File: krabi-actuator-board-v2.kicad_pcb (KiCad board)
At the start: 2 copper layers, 101.6 x 53.3 mm, 18 parts, among them J1 Power, J2 PWM, J3 Analog, J4 PWM, J5 Analog, J6 Communication, J7 Digital, J8 Conn_01x02_Pin

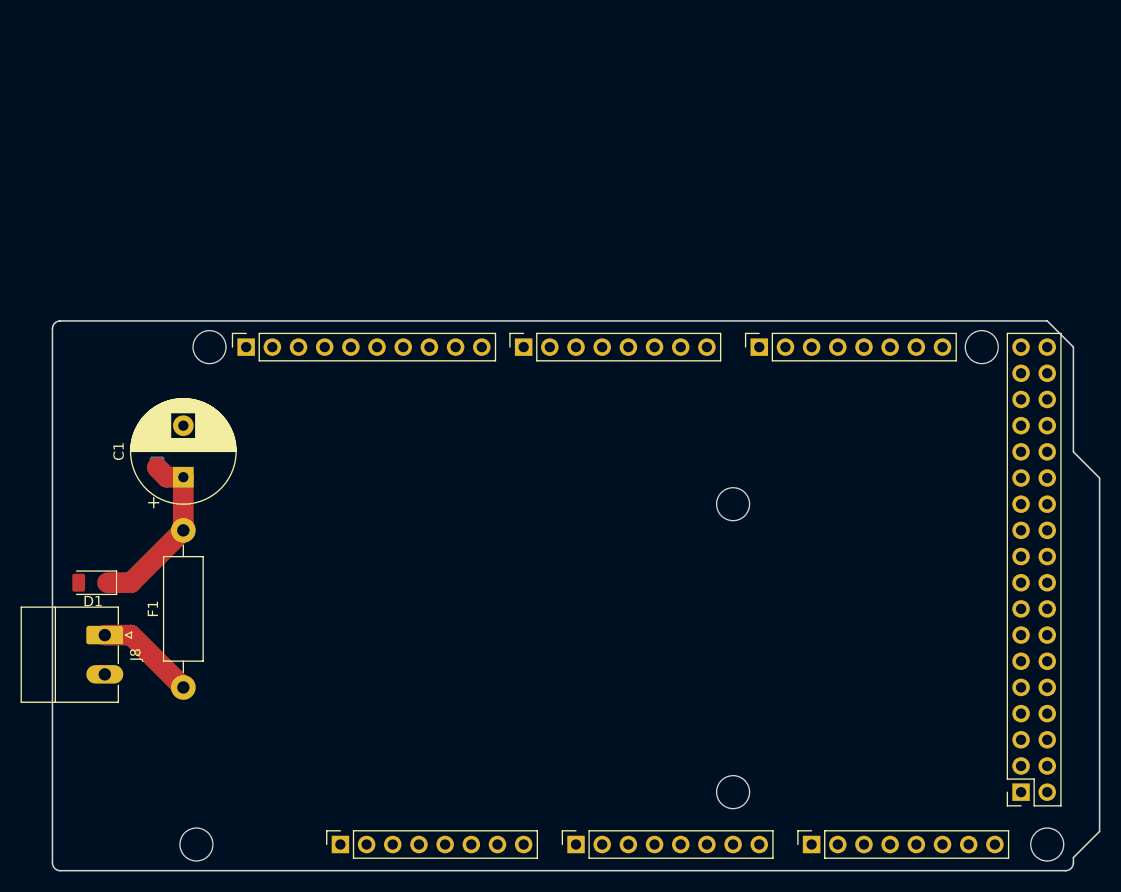
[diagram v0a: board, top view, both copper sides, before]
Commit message: Full command of the servos 6V power
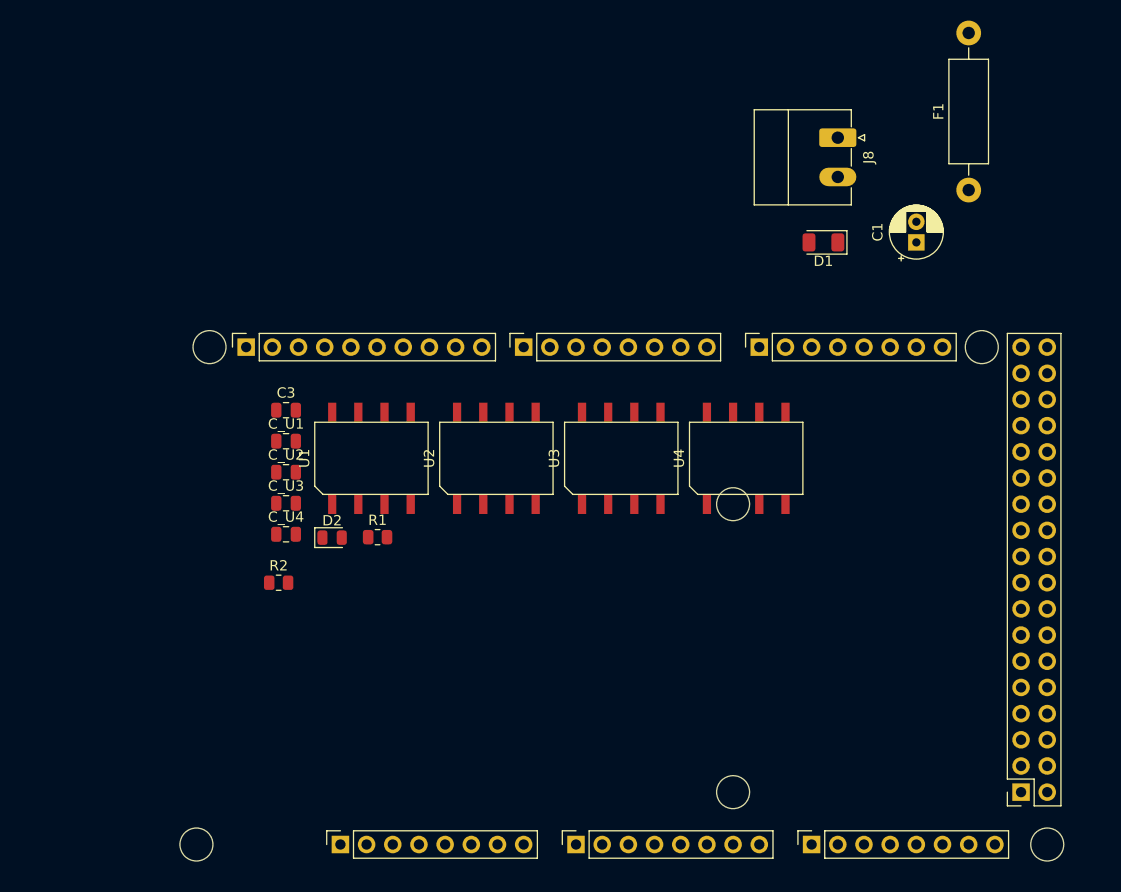
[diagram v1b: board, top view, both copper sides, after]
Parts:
- removed C2: C, Capacitor_SMD:C_0805_2012Metric
- added C3: 100nF, Capacitor_SMD:C_0805_2012Metric, F.Cu at (122.7, 55.3)
- added C_U1: 10pF, Capacitor_SMD:C_0805_2012Metric, F.Cu at (122.7, 58.3)
- added C_U2: 10pF, Capacitor_SMD:C_0805_2012Metric, F.Cu at (122.7, 61.3)
- added C_U3: 10pF, Capacitor_SMD:C_0805_2012Metric, F.Cu at (122.7, 64.3)
- added C_U4: 10pF, Capacitor_SMD:C_0805_2012Metric, F.Cu at (122.7, 67.4)
- added D2: LED, LED_SMD:LED_0805_2012Metric, F.Cu at (127.1, 67.7)
- added R1: 120, Resistor_SMD:R_0805_2012Metric, F.Cu at (131.5, 67.6)
- added R2: 0.01, Resistor_SMD:R_0805_2012Metric, F.Cu at (121.9, 72.1)
- added U1: XGZP6897D_differential_pressure_sensor, Krabi:SOIC-8-11mmx7mm outside pad 1.9, F.Cu at (130.9, 60.0)
- added U2: XGZP6897D_differential_pressure_sensor, Krabi:SOIC-8-11mmx7mm outside pad 1.9, F.Cu at (143.1, 60.0)
- added U3: XGZP6897D_differential_pressure_sensor, Krabi:SOIC-8-11mmx7mm outside pad 1.9, F.Cu at (155.2, 60.0)
- added U4: XGZP6897D_differential_pressure_sensor, Krabi:SOIC-8-11mmx7mm outside pad 1.9, F.Cu at (167.3, 60.0)
- C1: value 10µF -> 10mF; footprint Capacitor_THT:CP_Radial_D10.0mm_P5.00mm -> Capacitor_THT:CP_Radial_D5.0mm_P2.00mm
- moved F1 90.2 mm to (188.9, 34.0)
- moved J8 85.9 mm to (176.2, 28.9)
- moved D1 78.2 mm to (174.8, 39.0)
- moved C1 74.7 mm to (183.8, 39.0)
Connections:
- net /SCL/21 renamed SCL
- net /SDA/20 renamed SDA
- C1 pad 2: GNF_POWER -> GND
- D1 pad 2: GNF_POWER -> GND
- J8 pad 2: GNF_POWER -> GND
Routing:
- net 12_V: track 17.6 -> 0.00 mm
- net Net-(J8-Pin_1): track 9.72 -> 0.00 mm
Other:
- board outline removed

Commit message: Fixing bad association and symbols*
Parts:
- removed C_U3, C_U4: 10pF, Capacitor_SMD:C_0805_2012Metric
- removed U3, U4: XGZP6897D_differential_pressure_sensor, Krabi:SOIC-8-11mmx7mm outside pad 1.9
- added CFF_VR1: 3.3nF, Capacitor_SMD:C_0805_2012Metric, F.Cu at (-96.9, -99.1)
- added CFF_VR2: 3.3nF, Capacitor_SMD:C_0805_2012Metric, F.Cu at (-96.9, -96.1)
- added C_SV1: 100nF, Capacitor_SMD:C_0805_2012Metric, F.Cu at (-96.9, -93.1)
- added C_SV10: 100nF, Capacitor_SMD:C_0805_2012Metric, F.Cu at (-88.0, -96.1)
- added C_SV11: 100nF, Capacitor_SMD:C_0805_2012Metric, F.Cu at (-88.0, -93.1)
- added C_SV12: 100nF, Capacitor_SMD:C_0805_2012Metric, F.Cu at (-88.0, -90.1)
- added C_SV2: 100nF, Capacitor_SMD:C_0805_2012Metric, F.Cu at (-96.9, -90.1)
- added C_SV3: 100nF, Capacitor_SMD:C_0805_2012Metric, F.Cu at (-96.9, -87.1)
- added C_SV4: 100nF, Capacitor_SMD:C_0805_2012Metric, F.Cu at (-92.5, -99.1)
- added C_SV5: 100nF, Capacitor_SMD:C_0805_2012Metric, F.Cu at (-92.5, -96.1)
- added C_SV6: 100nF, Capacitor_SMD:C_0805_2012Metric, F.Cu at (-92.5, -93.1)
- added C_SV7: 100nF, Capacitor_SMD:C_0805_2012Metric, F.Cu at (-92.5, -90.1)
- added C_SV8: 100nF, Capacitor_SMD:C_0805_2012Metric, F.Cu at (-92.5, -87.1)
- added C_SV9: 100nF, Capacitor_SMD:C_0805_2012Metric, F.Cu at (-88.0, -99.1)
- added C_U5: 10pF, Capacitor_SMD:C_0805_2012Metric, F.Cu at (-85.0, -48.7)
- added C_U6: 10pF, Capacitor_SMD:C_0805_2012Metric, F.Cu at (-85.0, -45.7)
- added Cin_VR1: 470µF, Capacitor_THT:CP_Radial_D5.0mm_P2.00mm, F.Cu at (-83.4, -97.4)
- added Cin_VR2: 470µF, Capacitor_THT:CP_Radial_D5.0mm_P2.00mm, F.Cu at (-83.4, -90.8)
- added Cout_VR1: 470µF, Capacitor_THT:CP_Radial_D13.0mm_P5.00mm, F.Cu at (-126.6, -93.4)
- added Cout_VR2: 470µF, Capacitor_THT:CP_Radial_D13.0mm_P5.00mm, F.Cu at (-126.6, -78.8)
- added D1_VR1: 20V 5A, Diode_SMD:D_0805_2012Metric, F.Cu at (-83.8, -72.2)
- added D1_VR2: 20V 5A, Diode_SMD:D_0805_2012Metric, F.Cu at (-83.8, -69.1)
- added D3: LED, LED_SMD:LED_0805_2012Metric, F.Cu at (-83.8, -75.2)
- added D4: LED, LED_SMD:LED_0805_2012Metric, F.Cu at (-85.0, -42.7)
- added DS_PV1: D_Schottky 20V 1A, Diode_SMD:D_SMA, F.Cu at (-97.6, -36.7)
- added DS_PV2: D_Schottky 20V 1A, Diode_SMD:D_SMA, F.Cu at (-97.6, -32.2)
- added DS_PV3: D_Schottky 20V 1A, Diode_SMD:D_SMA, F.Cu at (-97.6, -27.6)
- added DS_PV4: D_Schottky 20V 1A, Diode_SMD:D_SMA, F.Cu at (-97.6, -23.1)
- added D_LS1: LED, LED_SMD:LED_0805_2012Metric, F.Cu at (-112.8, -37.5)
- added D_LS2: LED, LED_SMD:LED_0805_2012Metric, F.Cu at (-112.8, -34.4)
- added D_PV1: LED, LED_SMD:LED_0805_2012Metric, F.Cu at (-112.8, -31.4)
- added D_PV2: LED, LED_SMD:LED_0805_2012Metric, F.Cu at (-112.8, -28.3)
- added D_PV3: LED, LED_SMD:LED_0805_2012Metric, F.Cu at (-112.8, -25.3)
- added D_PV4: LED, LED_SMD:LED_0805_2012Metric, F.Cu at (-112.8, -22.3)
- added D_S1: LED, LED_SMD:LED_0805_2012Metric, F.Cu at (-112.8, -19.2)
- added D_S10: LED, LED_SMD:LED_0805_2012Metric, F.Cu at (-103.9, -34.4)
- added D_S11: LED, LED_SMD:LED_0805_2012Metric, F.Cu at (-103.9, -31.4)
- added D_S12: LED, LED_SMD:LED_0805_2012Metric, F.Cu at (-103.9, -28.3)
- added D_S2: LED, LED_SMD:LED_0805_2012Metric, F.Cu at (-108.4, -37.5)
- added D_S3: LED, LED_SMD:LED_0805_2012Metric, F.Cu at (-108.4, -34.4)
- added D_S4: LED, LED_SMD:LED_0805_2012Metric, F.Cu at (-108.4, -31.4)
- added D_S5: LED, LED_SMD:LED_0805_2012Metric, F.Cu at (-108.4, -28.3)
- added D_S6: LED, LED_SMD:LED_0805_2012Metric, F.Cu at (-108.4, -25.3)
- added D_S7: LED, LED_SMD:LED_0805_2012Metric, F.Cu at (-108.4, -22.3)
- added D_S8: LED, LED_SMD:LED_0805_2012Metric, F.Cu at (-108.4, -19.2)
- added D_S9: LED, LED_SMD:LED_0805_2012Metric, F.Cu at (-103.9, -37.5)
- added J_PV_1: ~, Connector_JST:JST_PH_B2B-PH-K_1x02_P2.00mm_Vertical, F.Cu at (-128.8, -59.9)
- added J_PV_2: ~, Connector_JST:JST_PH_B2B-PH-K_1x02_P2.00mm_Vertical, F.Cu at (-128.8, -53.3)
- added J_PV_3: ~, Connector_JST:JST_PH_B2B-PH-K_1x02_P2.00mm_Vertical, F.Cu at (-128.8, -46.8)
- added J_PV_4: ~, Connector_JST:JST_PH_B2B-PH-K_1x02_P2.00mm_Vertical, F.Cu at (-128.8, -40.2)
- added L1_VR1: 33µH, Krabi:BOURSPM5022, F.Cu at (-166.6, -57.2)
- added L1_VR2: 33µH, Krabi:BOURSPM5022, F.Cu at (-166.6, -42.1)
- added LED_VR1: LED, LED_SMD:LED_0805_2012Metric, F.Cu at (-83.8, -66.1)
- added LS1: Conn_01x02_Pin, Connector_JST:JST_PH_B2B-PH-K_1x02_P2.00mm_Vertical, F.Cu at (-128.8, -33.7)
- added LS2: Conn_01x02_Pin, Connector_JST:JST_PH_B2B-PH-K_1x02_P2.00mm_Vertical, F.Cu at (-128.8, -27.1)
- added MCP6N11_VR1: G10, Krabi:SOIC-8-1.27x5.4m, F.Cu at (-95.9, -72.5)
- added MCP6N11_VR2: G10, Krabi:SOIC-8-1.27x5.4m, F.Cu at (-89.4, -72.5)
- added Q_LS1: DMN2011UTS, Package_SO:TSSOP-8_4.4x3mm_P0.65mm, F.Cu at (-119.4, -60.3)
- added Q_LS2: DMN2011UTS, Package_SO:TSSOP-8_4.4x3mm_P0.65mm, F.Cu at (-119.4, -55.8)
- added Q_PV1: DMN2011UTS, Package_SO:TSSOP-8_4.4x3mm_P0.65mm, F.Cu at (-119.4, -51.2)
- added Q_PV2: DMN2011UTS, Package_SO:TSSOP-8_4.4x3mm_P0.65mm, F.Cu at (-119.4, -46.7)
- added Q_PV3: DMN2011UTS, Package_SO:TSSOP-8_4.4x3mm_P0.65mm, F.Cu at (-119.4, -42.1)
- added Q_PV4: DMN2011UTS, Package_SO:TSSOP-8_4.4x3mm_P0.65mm, F.Cu at (-119.4, -37.6)
- added R1_VR1: 38.8k, Resistor_SMD:R_0805_2012Metric, F.Cu at (-96.9, -84.1)
- added R1_VR2: 38.8k, Resistor_SMD:R_0805_2012Metric, F.Cu at (-96.9, -81.2)
- added R1_VR3: 50k, Resistor_SMD:R_0805_2012Metric, F.Cu at (-96.9, -78.2)
- added R1_VR4: 100, Resistor_SMD:R_0805_2012Metric, F.Cu at (-92.5, -84.1)
- added R2_VR1: 10k, Resistor_SMD:R_0805_2012Metric, F.Cu at (-92.5, -81.2)
- added R2_VR2: 10k, Resistor_SMD:R_0805_2012Metric, F.Cu at (-92.5, -78.2)
- added R3: 720, Resistor_SMD:R_0805_2012Metric, F.Cu at (-89.4, -48.8)
- added RB_LS1: 1.2k, Resistor_SMD:R_0805_2012Metric, F.Cu at (-112.9, -61.1)
- added RB_LS2: 1.2k, Resistor_SMD:R_0805_2012Metric, F.Cu at (-112.9, -58.2)
- added RB_ON_OFF_ALIM1: 6.65k, Resistor_SMD:R_0805_2012Metric, F.Cu at (-89.4, -45.8)
- added RF_VR1: 50k, Resistor_SMD:R_0805_2012Metric, F.Cu at (-88.1, -84.1)
- added RG_PV1: 50, Resistor_SMD:R_0805_2012Metric, F.Cu at (-112.9, -55.2)
- added RG_PV2: 50, Resistor_SMD:R_0805_2012Metric, F.Cu at (-112.9, -52.3)
- added RG_PV3: 50, Resistor_SMD:R_0805_2012Metric, F.Cu at (-112.9, -49.3)
- added RG_PV4: 50, Resistor_SMD:R_0805_2012Metric, F.Cu at (-112.9, -46.4)
- added RG_VR1: 100, Resistor_SMD:R_0805_2012Metric, F.Cu at (-88.1, -81.2)
- added RLED_LS1: 720, Resistor_SMD:R_0805_2012Metric, F.Cu at (-112.9, -43.4)
- added RLED_LS2: 720, Resistor_SMD:R_0805_2012Metric, F.Cu at (-112.9, -40.5)
- added RLED_PV1: 720, Resistor_SMD:R_0805_2012Metric, F.Cu at (-108.4, -61.1)
- added RLED_PV2: 720, Resistor_SMD:R_0805_2012Metric, F.Cu at (-108.4, -58.2)
- added RLED_PV3: 720, Resistor_SMD:R_0805_2012Metric, F.Cu at (-108.4, -55.2)
- added RLED_PV4: 720, Resistor_SMD:R_0805_2012Metric, F.Cu at (-108.4, -52.3)
- added RLED_S1: 320, Resistor_SMD:R_0805_2012Metric, F.Cu at (-108.4, -49.3)
- added RLED_S10: 320, Resistor_SMD:R_0805_2012Metric, F.Cu at (-104.0, -46.4)
- added RLED_S11: 320, Resistor_SMD:R_0805_2012Metric, F.Cu at (-104.0, -43.4)
- added RLED_S12: 320, Resistor_SMD:R_0805_2012Metric, F.Cu at (-104.0, -40.5)
- added RLED_S2: 320, Resistor_SMD:R_0805_2012Metric, F.Cu at (-108.4, -46.4)
- added RLED_S3: 320, Resistor_SMD:R_0805_2012Metric, F.Cu at (-108.4, -43.4)
- added RLED_S4: 320, Resistor_SMD:R_0805_2012Metric, F.Cu at (-108.4, -40.5)
- added RLED_S5: 320, Resistor_SMD:R_0805_2012Metric, F.Cu at (-104.0, -61.1)
- added RLED_S6: 320, Resistor_SMD:R_0805_2012Metric, F.Cu at (-104.0, -58.2)
- added RLED_S7: 320, Resistor_SMD:R_0805_2012Metric, F.Cu at (-104.0, -55.2)
- added RLED_S8: 320, Resistor_SMD:R_0805_2012Metric, F.Cu at (-104.0, -52.3)
- added RLED_S9: 320, Resistor_SMD:R_0805_2012Metric, F.Cu at (-104.0, -49.3)
- added RLED_VR1: 320, Resistor_SMD:R_0805_2012Metric, F.Cu at (-88.1, -78.2)
- added RMC_VR1: 10m (250mW), Resistor_SMD:R_1206_3216Metric, F.Cu at (-83.1, -83.9)
- added RMC_VR2: 10m (250mW), Resistor_SMD:R_1206_3216Metric, F.Cu at (-83.1, -80.7)
- added RPD_PV1: 10k, Resistor_SMD:R_0805_2012Metric, F.Cu at (-99.6, -61.1)
- added RPD_PV2: 10k, Resistor_SMD:R_0805_2012Metric, F.Cu at (-99.6, -58.2)
- added RPD_PV3: 10k, Resistor_SMD:R_0805_2012Metric, F.Cu at (-99.6, -55.2)
- added RPD_PV4: 10k, Resistor_SMD:R_0805_2012Metric, F.Cu at (-99.6, -52.3)
- added RPU_ON_OFF_ALIM1: 20k, Resistor_SMD:R_0805_2012Metric, F.Cu at (-89.4, -42.9)
- added RT_ON_OFF_ALIM1: 20k, Resistor_SMD:R_0805_2012Metric, F.Cu at (-89.4, -39.9)
- added SV1: Conn_01x03_Pin, Connector_PinSocket_2.54mm:PinSocket_1x03_P2.54mm_Vertical, F.Cu at (-129.4, -108.0)
- added SV10: Conn_01x03_Pin, Connector_PinSocket_2.54mm:PinSocket_1x03_P2.54mm_Vertical, F.Cu at (-88.0, -108.0)
- added SV11: Conn_01x03_Pin, Connector_PinSocket_2.54mm:PinSocket_1x03_P2.54mm_Vertical, F.Cu at (-83.4, -108.0)
- added SV12: Conn_01x03_Pin, Connector_PinSocket_2.54mm:PinSocket_1x03_P2.54mm_Vertical, F.Cu at (-78.8, -108.0)
- added SV2: Conn_01x03_Pin, Connector_PinSocket_2.54mm:PinSocket_1x03_P2.54mm_Vertical, F.Cu at (-124.8, -108.0)
- added SV3: Conn_01x03_Pin, Connector_PinSocket_2.54mm:PinSocket_1x03_P2.54mm_Vertical, F.Cu at (-120.2, -108.0)
- added SV4: Conn_01x03_Pin, Connector_PinSocket_2.54mm:PinSocket_1x03_P2.54mm_Vertical, F.Cu at (-115.6, -108.0)
- added SV5: Conn_01x03_Pin, Connector_PinSocket_2.54mm:PinSocket_1x03_P2.54mm_Vertical, F.Cu at (-111.0, -108.0)
- added SV6: Conn_01x03_Pin, Connector_PinSocket_2.54mm:PinSocket_1x03_P2.54mm_Vertical, F.Cu at (-106.4, -108.0)
- added SV7: Conn_01x03_Pin, Connector_PinSocket_2.54mm:PinSocket_1x03_P2.54mm_Vertical, F.Cu at (-101.8, -108.0)
- added SV8: Conn_01x03_Pin, Connector_PinSocket_2.54mm:PinSocket_1x03_P2.54mm_Vertical, F.Cu at (-97.2, -108.0)
- added SV9: Conn_01x03_Pin, Connector_PinSocket_2.54mm:PinSocket_1x03_P2.54mm_Vertical, F.Cu at (-92.6, -108.0)
- added U5: XGZP6897D_differential_pressure_sensor, Krabi:SOIC-8-11mmx7mm outside pad 1.9, F.Cu at (-85.6, -56.4)
- added U6: XGZP6897D_differential_pressure_sensor, Krabi:SOIC-8-11mmx7mm outside pad 1.9, F.Cu at (-73.4, -56.4)
- added VR1: LM2596s, Package_TO_SOT_SMD:TO-263-5_TabPin6, F.Cu at (-106.1, -94.5)
- added VR2: LM2596s, Package_TO_SOT_SMD:TO-263-5_TabPin6, F.Cu at (-106.1, -82.1)
- C1: value 10mF -> 1mF; footprint Capacitor_THT:CP_Radial_D5.0mm_P2.00mm -> Capacitor_THT:CP_Radial_D16.0mm_P7.50mm
- R1: value 120 -> 253
- R2: value 0.01 -> 320
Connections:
- net 12_V renamed 12V
- J2 pad 10: /*8 -> SERVO_8
- J2 pad 6: /*12 -> SERVO_12
- J2 pad 7: /*11 -> SERVO_11
- J2 pad 8: /*10 -> SERVO_10
- J2 pad 9: /*9 -> SERVO_9
- J3 pad 1: /A0 -> CURRENT_VR2
- J3 pad 2: /A1 -> CURRENT_VR1
- J4 pad 1: /*7 -> SERVO_7
- J4 pad 2: /*6 -> ON/OFF
- J4 pad 3: /*5 -> SERVO_6
- J4 pad 4: /*4 -> SERVO_5
- J4 pad 5: /*3 -> SERVO_4
- J4 pad 6: /*2 -> SERVO_3
- J4 pad 7: /TX0/1 -> SERVO_2
- J4 pad 8: /RX0/0 -> SERVO_1
- J7 pad 20: /37 -> LEDS_2
- J7 pad 22: /35 -> LEDS_1
- J7 pad 31: /24 -> CON_PV3
- J7 pad 32: /25 -> CON_PV4
- J7 pad 33: /22 -> CON_PV1
- J7 pad 34: /23 -> CON_PV2
- R2 pad 1: GND_POWER -> Net-(D3-A)
